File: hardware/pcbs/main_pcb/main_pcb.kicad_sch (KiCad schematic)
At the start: 17 parts, among them J5 Conn_01x06, SW1 SW_Push, U5 ATmega2560-16A

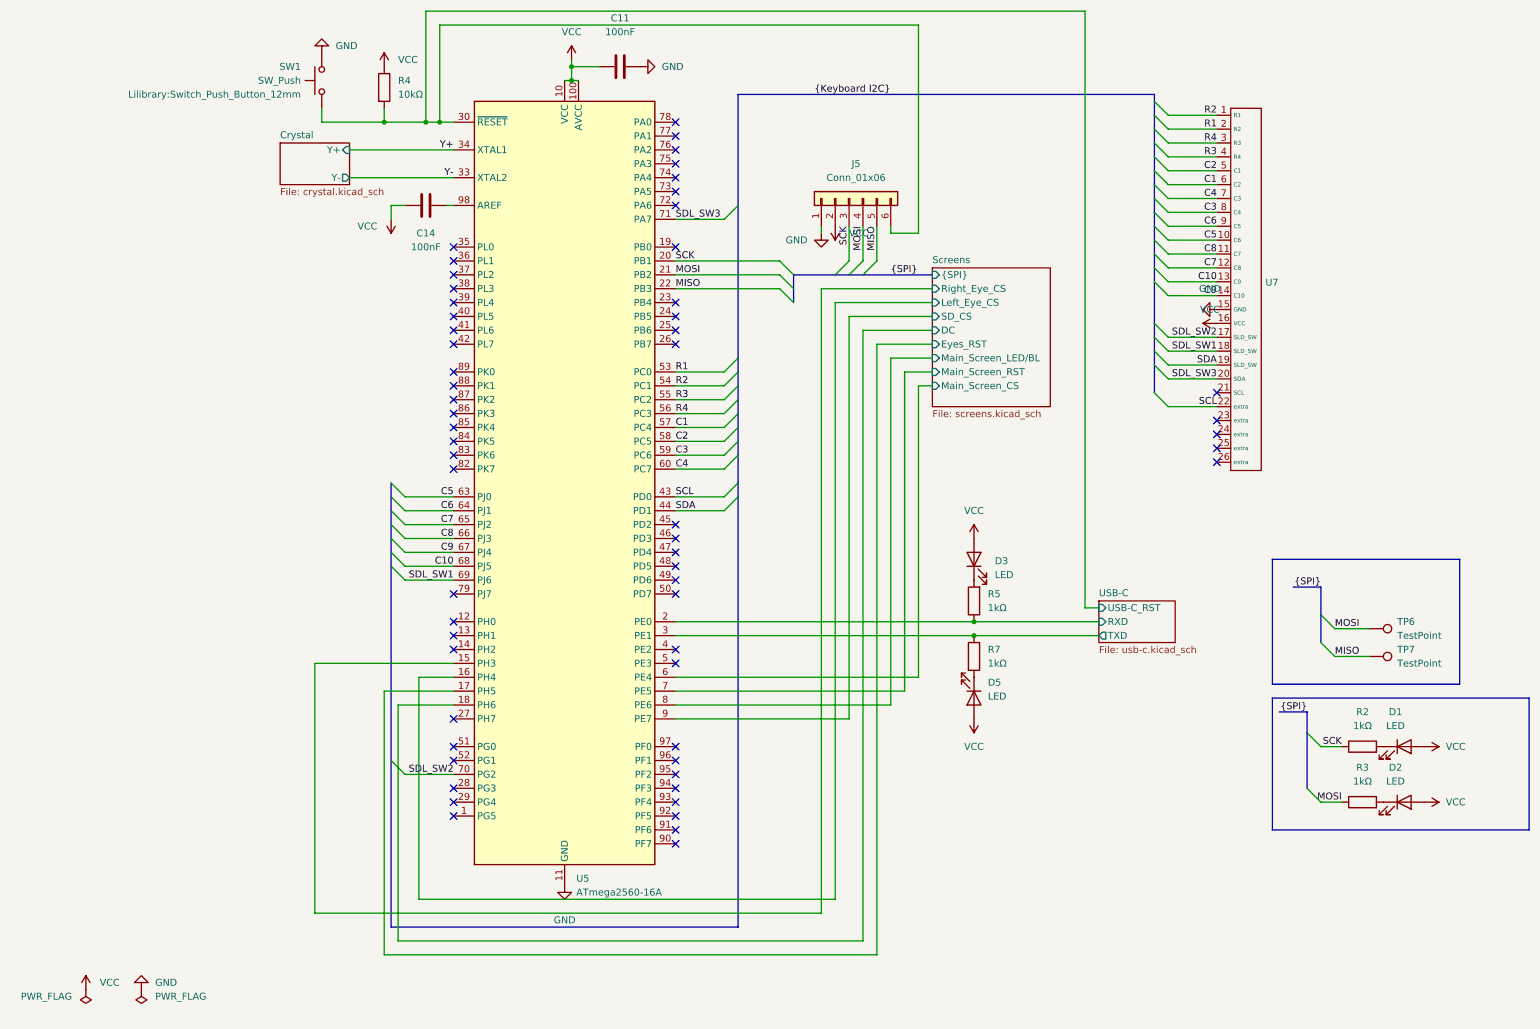
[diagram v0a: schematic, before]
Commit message: Maddie/main pcb schematic cleaning (#88)
* feat(main PCB): Reworks schematic

* feat(main PCB): Removes no longer used BL pin 01x02 header

* feat(main PCB): Fixes main PCB routing issue

* chore: Reworks main PCB schematic/PCB

* chore: Removes old csv file
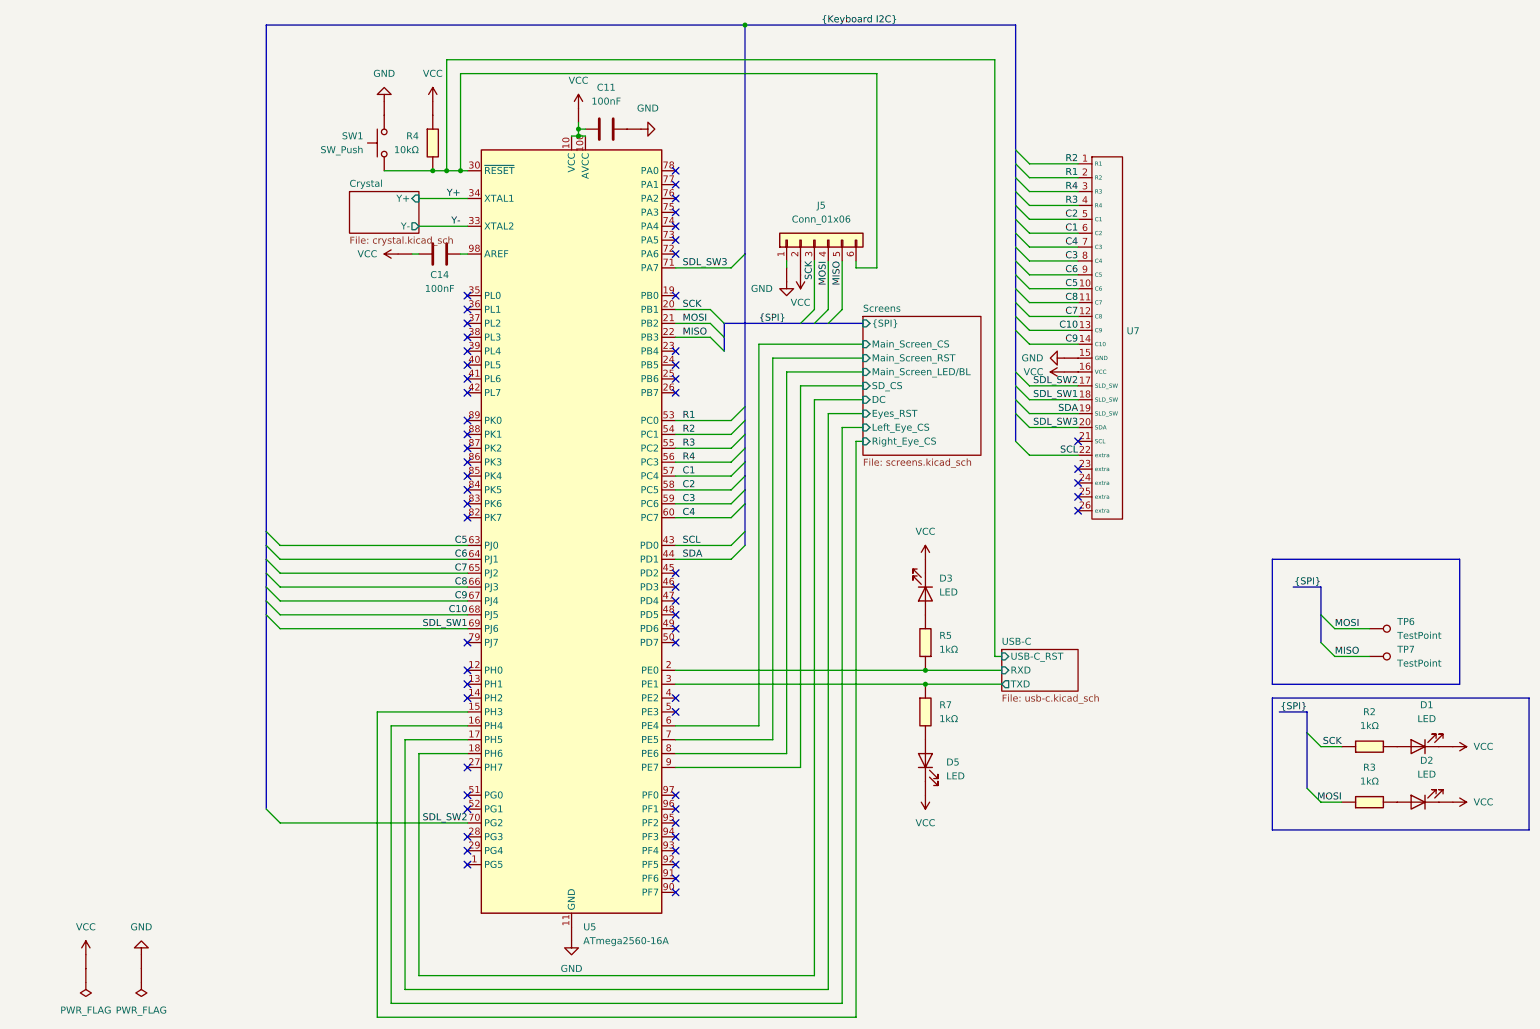
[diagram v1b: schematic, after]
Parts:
- C11, C14: symbol Device:C -> Lilybrary:Capacitor
- D1, D2, D3, D5: symbol Device:LED -> Lilybrary:LED
- J5: symbol Connector_Generic:Conn_01x06 -> Lilybrary:Conn_01x06
- R2, R3, R4, R5, R7: symbol Device:R -> Lilybrary:Resistor
- SW1: symbol Switch:SW_Push -> Lilybrary:SW_Push
- TP6, TP7: symbol Connector:TestPoint -> Lilybrary:TestPoint
- U5: footprint Package_QFP:TQFP-100_14x14mm_P0.5mm -> Lilibrary:ATmega2560-16AU; symbol MCU_Microchip_ATmega:ATmega2560-16A -> Lilybrary:ATmega2560-16A
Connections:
- net VCC: now also D1.1 (K), D2.1 (K), D3.1 (K), D5.1 (K); no longer D1.2 (A), D2.2 (A), D3.2 (A), D5.2 (A)
- net at R5.2: now also D3.2 (A); no longer D3.1 (K)
- net at R2.2: now also D1.2 (A); no longer D1.1 (K)
- net at R7.2: now also D5.2 (A); no longer D5.1 (K)
- net at R3.2: now also D2.2 (A); no longer D2.1 (K)
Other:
- company: (none) -> Lily's Pad
- title: (none) -> Main PCB
- moved on the sheet: C11, C14, D1, D2, D3, D5, J5, SW1, U5, U7
